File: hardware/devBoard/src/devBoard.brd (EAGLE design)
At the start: 65.5 x 56.1 mm, 82 parts, among them IC1 OPA344, IC2 FT230XS, IC3 Hall, IC4 OPA344, IC6 LM4862, J3 MICRO-SD_CARD_SOCKET, Q1 2N2222, X1 USBSMD

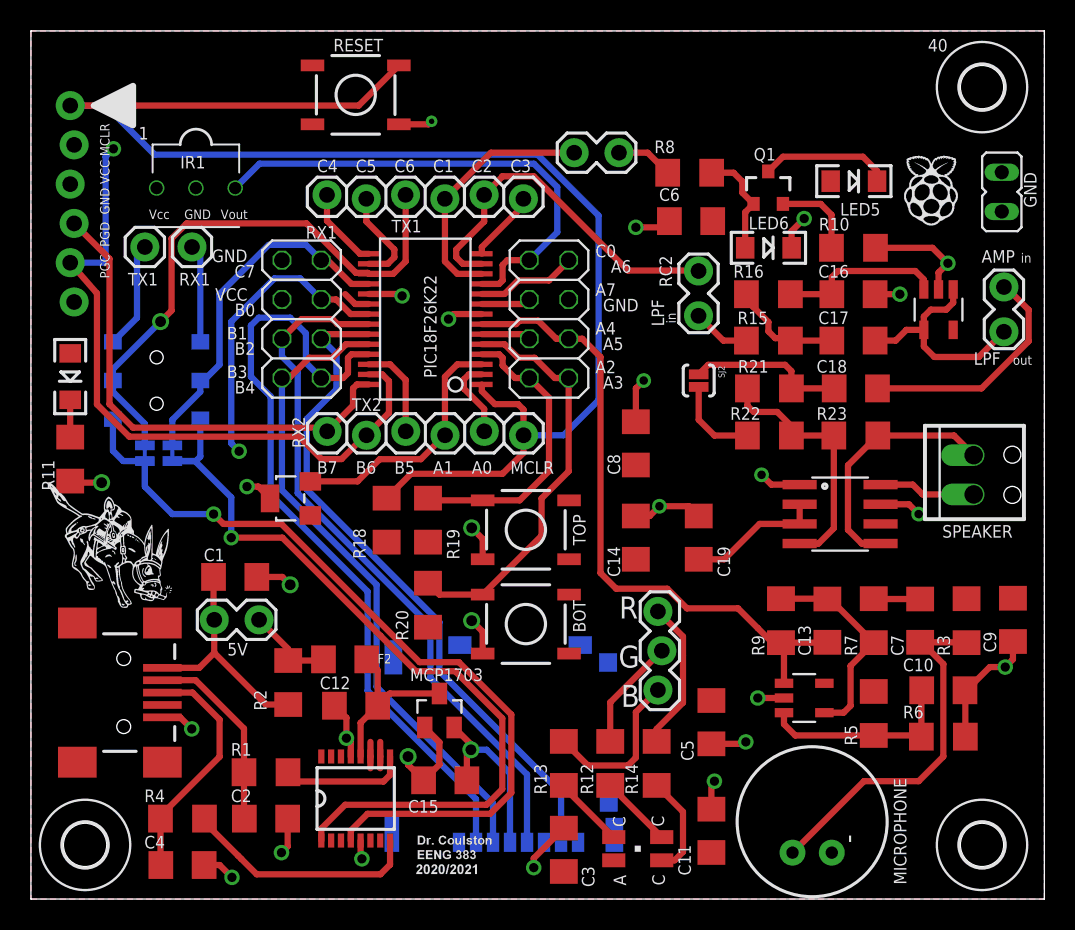
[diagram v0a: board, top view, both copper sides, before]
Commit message: updated QR code to gitHub URL
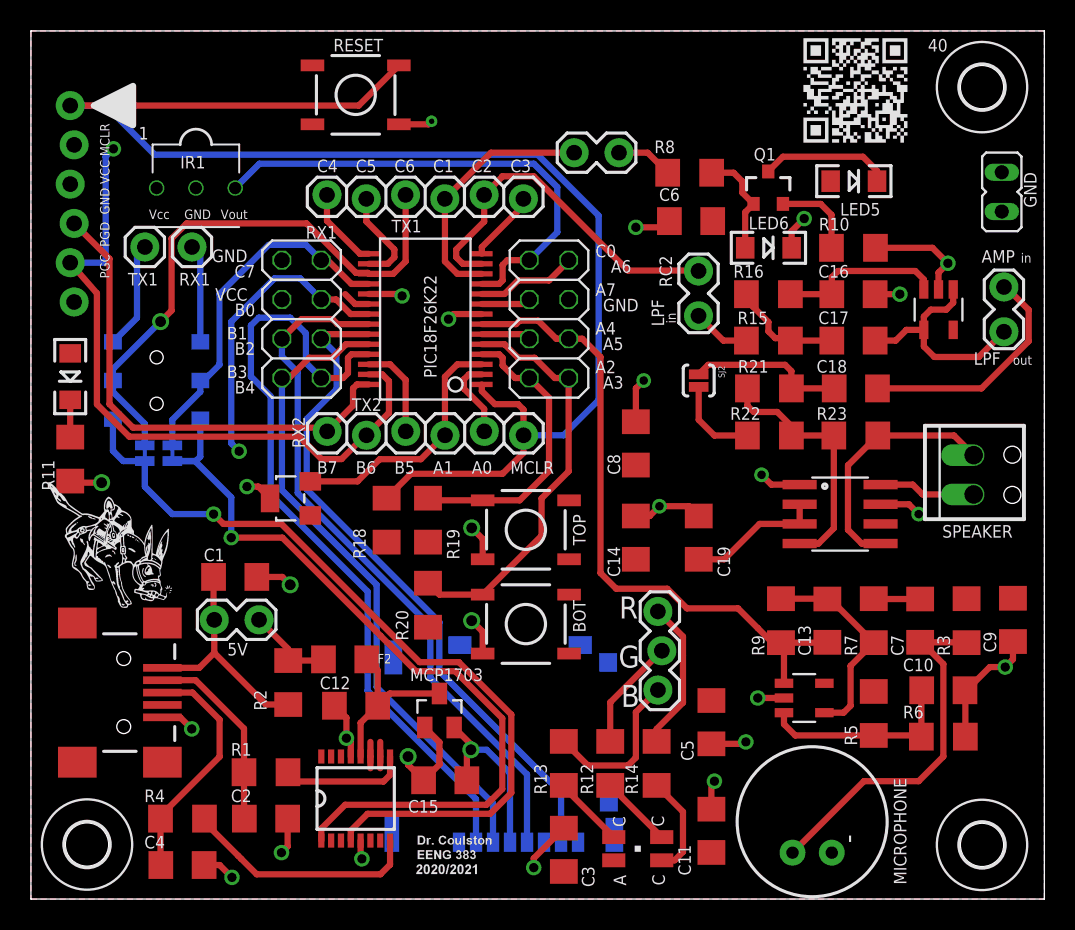
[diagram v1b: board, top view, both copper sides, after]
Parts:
- moved H4 0.13 mm to (3.63, 3.53)
